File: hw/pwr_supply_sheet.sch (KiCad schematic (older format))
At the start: 15 parts

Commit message: PCB was too big for itead, reduced size and ordered one
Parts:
- C10, C12: footprint usevolt:usevolt-CAP_EEE-FK1H470P -> usevolt:CAP_EEE-FK1H470P
- D1: footprint usevolt:usevolt-DO-214AA -> usevolt:DO-214AA
- D2: footprint usevolt:usevolt-DO219AB -> usevolt:DO219AB
- F1: footprint usevolt:usevolt-FUSE_MC36211 -> usevolt:FUSE_MC36211
- L1: footprint usevolt:usevolt-INDUCTOR_BOURNS_10X13X5MM -> usevolt:INDUCTOR_BOURNS_10X13X5MM
- VR1: footprint usevolt:usevolt-SOIC8 -> usevolt:SOIC8
- VR2: footprint usevolt:usevolt-SOT-23_3-PIN -> usevolt:SOT-23_3-PIN
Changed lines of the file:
@@
 F 0 "F1" H 2600 4054 45  0000 C CNN
 F 1 "FUSE_MC36211_350MA" H 2600 3970 45  0000 C CNN
-F 2 "usevolt:usevolt-FUSE_MC36211" H 2630 4000 20  0001 C CNN
+F 2 "usevolt:FUSE_MC36211" H 2630 4000 20  0001 C CNN
 F 3 "http://www.farnell.com/datasheets/1678471.pdf?_ga=1.218604761.1948984246.1460023966" H 2720 3870 60  0001 C CNN
 F 4 "Farnell" H 3020 4170 60  0001 C CNN "1st Source"
@@
 F 0 "D1" V 3092 3982 45  0000 R CNN
 F 1 "DIODE_TVS_SMBJ33A-TRDO-214AA" V 3008 3982 45  0000 R CNN
-F 2 "usevolt:usevolt-DO-214AA" H 3030 4200 20  0001 C CNN
+F 2 "usevolt:DO-214AA" H 3030 4200 20  0001 C CNN
 F 3 "http://www.littelfuse.com/~/media/electronics/datasheets/tvs_diodes/littelfuse_tvs_diode_smbj_datasheet.pdf.pdf" H 3110 4060 60  0001 C CNN
 F 4 "Digi-Key" H 3410 4360 60  0001 C CNN "1st Source"
@@
 F 0 "C10" V 3308 4153 45  0000 L CNN
 F 1 "CAP_EEE-FK1H470P" V 3392 4153 45  0000 L CNN
-F 2 "usevolt:usevolt-CAP_EEE-FK1H470P" H 3430 4200 20  0001 C CNN
+F 2 "usevolt:CAP_EEE-FK1H470P" H 3430 4200 20  0001 C CNN
 F 3 "http://industrial.panasonic.com/www-cgi/jvcr13pz.cgi?E+PZ+3+ABA0120+EEEFK1H470P+7+WW" H 3400 3990 60  0001 C CNN
 F 4 "667-EEE-FK1H470P" H 4000 4590 60  0001 C CNN "2nd Source Part Number"
@@
 F 0 "VR1" H 5050 4804 45  0000 C CNN
 F 1 "LM2671SOIC8" H 5050 4720 45  0000 C CNN
-F 2 "usevolt:usevolt-SOIC8" H 4880 4300 20  0001 C CNN
+F 2 "usevolt:SOIC8" H 4880 4300 20  0001 C CNN
 F 3 "http://www.farnell.com/datasheets/1902681.pdf?_ga=1.246738500.1948984246.1460023966" H 4650 4670 60  0001 C CNN
 F 4 "1469200" H 5050 5070 60  0001 C CNN "1st Source Part Number"
@@
 F 0 "D2" V 6150 3852 45  0000 R CNN
 F 1 "DIODE_RS07J-GS18" H 6220 3890 45  0001 L BNN
-F 2 "usevolt:usevolt-DO219AB" H 6230 4100 20  0001 C CNN
+F 2 "usevolt:DO219AB" H 6230 4100 20  0001 C CNN
 F 3 "http://www.vishay.com/docs/85742/rs07b.pdf" H 6220 3970 60  0001 C CNN
 F 4 "1864882" H 6820 4570 60  0001 C CNN "2nd Source Part Number"
@@
 F 0 "L1" H 6500 4041 45  0000 C CNN
 F 1 "INDUCTOR_SDR1005-101KL" H 6500 3957 45  0000 C CNN
-F 2 "usevolt:usevolt-INDUCTOR_BOURNS_10X13X5MM" H 6530 4000 20  0001 C CNN
+F 2 "usevolt:INDUCTOR_BOURNS_10X13X5MM" H 6530 4000 20  0001 C CNN
 F 3 "http://www.farnell.com/datasheets/1695384.pdf?_ga=1.223340891.1948984246.1460023966" H 6400 3790 60  0001 C CNN
 F 4 "1828057" H 6800 4190 60  0001 C CNN "1st Source Part Number"
@@
 F 0 "C12" V 6758 4153 45  0000 L CNN
 F 1 "CAP_EEE-FK1H470P" V 6842 4153 45  0000 L CNN
-F 2 "usevolt:usevolt-CAP_EEE-FK1H470P" H 6880 4200 20  0001 C CNN
+F 2 "usevolt:CAP_EEE-FK1H470P" H 6880 4200 20  0001 C CNN
 F 3 "http://industrial.panasonic.com/www-cgi/jvcr13pz.cgi?E+PZ+3+ABA0120+EEEFK1H470P+7+WW" H 6850 3990 60  0001 C CNN
 F 4 "667-EEE-FK1H470P" H 7450 4590 60  0001 C CNN "2nd Source Part Number"
@@
 F 0 "VR2" H 8000 4305 45  0000 C CNN
 F 1 "REG_MCP1700" H 8000 3950 45  0001 L BNN
-F 2 "usevolt:usevolt-SOT-23_3-PIN" H 8030 4100 20  0001 C CNN
+F 2 "usevolt:SOT-23_3-PIN" H 8030 4100 20  0001 C CNN
 F 3 "http://www.farnell.com/datasheets/1784514.pdf?_ga=1.221693144.1948984246.1460023966" H 7700 4270 60  0001 C CNN
 F 4 "1296592" H 8100 4670 60  0001 C CNN "1st Source Part Number"

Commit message: starting to design hw 5.0, with variable current source for LCD backlight
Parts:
- removed C10, C12: CAP_EEE-FK1H470P, usevolt:CAP_EEE-FK1H470P, symbol CAP_EEE-FK1H470P
- removed D3: WL-SMCW-150060BS75000-B, wurth_LEDS:Wuerth_Elektronik_LEDs_rev15b-0603, symbol WL-SMCW-150060BS75000-B
- removed L1: INDUCTOR_SDR1005-101KL, usevolt:INDUCTOR_BOURNS_10X13X5MM, symbol INDUCTOR_SDR1005-101KL
- removed R4: 470, multicomp:Multicomp-RESC1608X60N, symbol 470
- added C201, C202: T491D226K035AT, kemet:7343, symbol T491D226K035AT
- added L201: IND_744045210, usevolt:IND_744045210, symbol IND_744045210
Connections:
- wire segments 31 -> 29
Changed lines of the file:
@@
 P 3000 4050
 F 0 "D1" V 3092 3982 45  0000 R CNN
-F 1 "DIODE_TVS_SMBJ33A-TRDO-214AA" V 3008 3982 45  0000 R CNN
+F 1 "DIODE_TVS_SMBJ33A-TRDO-214AA" V 2950 5150 45  0000 R CNN
 F 2 "usevolt:DO-214AA" H 3030 4200 20  0001 C CNN
 F 3 "http://www.littelfuse.com/~/media/electronics/datasheets/tvs_diodes/littelfuse_tvs_diode_smbj_datasheet.pdf.pdf" H 3110 4060 60  0001 C CNN
@@
 F 7 "KEMET" H 3204 4059 60  0001 C CNN "Manufacturer"
 	1    3200 3950
-	0    1    1    0
-$EndComp
-$Comp
-L CAP_EEE-FK1H470P C10
-U 1 1 57B821E6
-P 3400 4050
-F 0 "C10" V 3308 4153 45  0000 L CNN
-F 1 "CAP_EEE-FK1H470P" V 3392 4153 45  0000 L CNN
-F 2 "usevolt:CAP_EEE-FK1H470P" H 3430 4200 20  0001 C CNN
-F 3 "http://industrial.panasonic.com/www-cgi/jvcr13pz.cgi?E+PZ+3+ABA0120+EEEFK1H470P+7+WW" H 3400 3990 60  0001 C CNN
-F 4 "667-EEE-FK1H470P" H 4000 4590 60  0001 C CNN "2nd Source Part Number"
-F 5 "Digi-Key" H 3700 4290 60  0001 C CNN "1st Source"
-F 6 "EEE-FK1H470P" H 3600 4190 60  0001 C CNN "Manufacturer Part Number"
-F 7 "Mouser" H 3900 4490 60  0001 C CNN "2nd Source"
-F 8 "Panasonic Electronic Components" H 3500 4090 60  0001 C CNN "Manufacturer"
-F 9 "PCE3815CT-ND" H 3800 4390 60  0001 C CNN "1st Source Part Number"
-	1    3400 4050
 	0    1    1    0
 $EndComp
@@
 $EndComp
 $Comp
-L INDUCTOR_SDR1005-101KL L1
-U 1 1 57B82455
-P 6500 3850
-F 0 "L1" H 6500 4041 45  0000 C CNN
-F 1 "INDUCTOR_SDR1005-101KL" H 6500 3957 45  0000 C CNN
-F 2 "usevolt:INDUCTOR_BOURNS_10X13X5MM" H 6530 4000 20  0001 C CNN
-F 3 "http://www.farnell.com/datasheets/1695384.pdf?_ga=1.223340891.1948984246.1460023966" H 6400 3790 60  0001 C CNN
-F 4 "1828057" H 6800 4190 60  0001 C CNN "1st Source Part Number"
-F 5 "BOURNS" H 6500 3890 60  0001 C CNN "Manufacturer"
-F 6 "Digi-Key" H 6900 4290 60  0001 C CNN "2nd Source"
-F 7 "Farnell" H 6700 4090 60  0001 C CNN "1st Source"
-F 8 "SDR1005-101KL" H 6600 3990 60  0001 C CNN "Manufacturer Part Number"
-F 9 "SDR1005-101KLCT-ND" H 7000 4390 60  0001 C CNN "2nd Source Part Number"
-	1    6500 3850
-	1    0    0    -1
-$EndComp
-$Comp
-L CAP_EEE-FK1H470P C12
-U 1 1 57B827AB
-P 6850 4050
-F 0 "C12" V 6758 4153 45  0000 L CNN
-F 1 "CAP_EEE-FK1H470P" V 6842 4153 45  0000 L CNN
-F 2 "usevolt:CAP_EEE-FK1H470P" H 6880 4200 20  0001 C CNN
-F 3 "http://industrial.panasonic.com/www-cgi/jvcr13pz.cgi?E+PZ+3+ABA0120+EEEFK1H470P+7+WW" H 6850 3990 60  0001 C CNN
-F 4 "667-EEE-FK1H470P" H 7450 4590 60  0001 C CNN "2nd Source Part Number"
-F 5 "Digi-Key" H 7150 4290 60  0001 C CNN "1st Source"
-F 6 "EEE-FK1H470P" H 7050 4190 60  0001 C CNN "Manufacturer Part Number"
-F 7 "Mouser" H 7350 4490 60  0001 C CNN "2nd Source"
-F 8 "Panasonic Electronic Components" H 6950 4090 60  0001 C CNN "Manufacturer"
-F 9 "PCE3815CT-ND" H 7250 4390 60  0001 C CNN "1st Source Part Number"
-	1    6850 4050
-	0    1    1    0
-$EndComp
-$Comp
 L REG_MCP1700 VR2
 U 1 1 57B82857
@@
 	0    1    1    0
 $EndComp
-$Comp
-L 470 R4
-U 1 1 57B82ADF
-P 8850 3850
-F 0 "R4" V 8858 3908 45  0000 L CNN
-F 1 "470" V 8942 3908 45  0000 L CNN
-F 2 "multicomp:Multicomp-RESC1608X60N" H 8880 4000 20  0001 C CNN
-F 3 "" H 8819 3889 60  0001 C CNN
-F 4 "9331239" H 9219 4289 60  0001 C CNN "1st Source Part Number"
-F 5 "Farnell" H 9119 4189 60  0001 C CNN "1st Source"
-F 6 "MC0063W06031470R" H 9019 4089 60  0001 C CNN "Manufacturer Part Number"
-F 7 "MULTICOMP" H 8919 3989 60  0001 C CNN "Manufacturer"
-	1    8850 3850
-	0    1    1    0
-$EndComp
-$Comp
-L WL-SMCW-150060BS75000-B D3
-U 1 1 57B82B6E
-P 8850 4200
-F 0 "D3" V 8850 4132 45  0000 R CNN
-F 1 "WL-SMCW-150060BS75000-B" H 9050 4300 45  0001 L BNN
-F 2 "wurth_LEDS:Wuerth_Elektronik_LEDs_rev15b-0603" H 8880 4350 20  0001 C CNN
-F 3 "http://www.farnell.com/datasheets/1911343.pdf?_ga=1.259491274.1948984246.1460023966" H 8650 4400 60  0001 C CNN
-F 4 "150060BS75000" H 9059 4403 60  0001 C CNN "Manufacturer Part Number"
-F 5 "2322069" H 9259 4603 60  0001 C CNN "1st Source Part Number"
-F 6 "Farnell" H 9159 4503 60  0001 C CNN "1st Source"
-F 7 "WURTH ELEKTRONIK" H 8959 4303 60  0001 C CNN "Manufacturer"
-	1    8850 4200
-	0    -1   -1   0
-$EndComp
-Wire Wire Line
-	8850 4100 8850 4050
-Wire Wire Line
-	2900 4300 8850 4300
 Wire Wire Line
 	8000 4300 8000 4250
@@
 Connection ~ 3200 3850
 Wire Wire Line
-	8600 4150 8600 4300
-Connection ~ 8600 4300
-Wire Wire Line
-	8850 3750 8600 3750
-Wire Wire Line
 	8600 3600 8600 3850
 Wire Wire Line
@@
 	3400 3550 3400 3850
 $Comp
-L VDD #PWR020
+L VDD #PWR201
 U 1 1 57B83157
 P 3400 3550
-F 0 "#PWR020" H 3400 3400 50  0001 C CNN
+F 0 "#PWR201" H 3400 3400 50  0001 C CNN
 F 1 "VDD" H 3417 3723 50  0000 C CNN
 F 2 "" H 3400 3550 50  0000 C CNN
@@
 Connection ~ 3400 3750
 $Comp
-L +5V #PWR021
+L +5V #PWR204
 U 1 1 57B831F8
 P 6850 3600
-F 0 "#PWR021" H 6850 3450 50  0001 C CNN
+F 0 "#PWR204" H 6850 3450 50  0001 C CNN
 F 1 "+5V" H 6865 3773 50  0000 C CNN
 F 2 "" H 6850 3600 50  0000 C CNN
@@
 Connection ~ 6850 3750
 $Comp
-L +3V3 #PWR022
+L +3V3 #PWR205
 U 1 1 57B83259
 P 8600 3600
-F 0 "#PWR022" H 8600 3450 50  0001 C CNN
+F 0 "#PWR205" H 8600 3450 50  0001 C CNN
 F 1 "+3V3" H 8615 3773 50  0000 C CNN
 F 2 "" H 8600 3600 50  0000 C CNN
@@
 	1    0    0    -1
 $EndComp
-Connection ~ 8600 3750
 Wire Wire Line
 	2400 3850 2150 3850
@@
 NoConn ~ 4550 4050
 $Comp
-L VDD #PWR023
+L VDD #PWR202
 U 1 1 57B9C56A
 P 3800 2100
-F 0 "#PWR023" H 3800 1950 50  0001 C CNN
+F 0 "#PWR202" H 3800 1950 50  0001 C CNN
 F 1 "VDD" H 3817 2273 50  0000 C CNN
 F 2 "" H 3800 2100 50  0000 C CNN
@@
 $EndComp
 $Comp
-L PWR_FLAG #FLG024
+L PWR_FLAG #FLG201
 U 1 1 57B9C59C
 P 3800 2300
-F 0 "#FLG024" H 3800 2395 50  0001 C CNN
+F 0 "#FLG201" H 3800 2395 50  0001 C CNN
 F 1 "PWR_FLAG" H 3800 2523 50  0000 C CNN
 F 2 "" H 3800 2300 50  0000 C CNN
@@
 	3800 2300 3800 2100
 $Comp
-L GND #PWR025
+L GND #PWR203
 U 1 1 57B9D351
 P 4300 2350
-F 0 "#PWR025" H 4300 2100 50  0001 C CNN
+F 0 "#PWR203" H 4300 2100 50  0001 C CNN
 F 1 "GND" H 4305 2177 50  0000 C CNN
 F 2 "" H 4300 2350 50  0000 C CNN
@@
 $EndComp
 $Comp
-L PWR_FLAG #FLG026
+L PWR_FLAG #FLG202
 U 1 1 57B9D3A1
 P 4300 2150
-F 0 "#FLG026" H 4300 2245 50  0001 C CNN
+F 0 "#FLG202" H 4300 2245 50  0001 C CNN
 F 1 "PWR_FLAG" H 4300 2374 50  0000 C CNN
 F 2 "" H 4300 2150 50  0000 C CNN
@@
 Wire Wire Line
 	4300 2150 4300 2350
+Wire Wire Line
+	8600 4150 8600 4300
+Wire Wire Line
+	8600 4300 2900 4300
+$Comp
+L IND_744045210 L201
+U 1 1 58F3C600
+P 6500 3850
+F 0 "L201" H 6650 3900 45  0000 C CNN
+F 1 "IND_744045210" H 6500 3800 45  0000 C CNN
+F 2 "usevolt:IND_744045210" H 6530 4000 20  0001 C CNN
+F 3 "http://www.farnell.com/datasheets/1735442.pdf?_ga=1.223184091.1948984246.1460023966" H 6400 3790 60  0001 C CNN
+F 4 "1800416" H 6800 4190 60  0001 C CNN "1st Source Part Number"
+F 5 "WURTH ELEKTRONIK" H 6500 3890 60  0001 C CNN "Manufacturer"
+F 6 "Digi-Key" H 6900 4290 60  0001 C CNN "2nd Source"
+F 7 "Farnell" H 6700 4090 60  0001 C CNN "1st Source"
+F 8 "744045210" H 6600 3990 60  0001 C CNN "Manufacturer Part Number"
+F 9 "732-3072-1-ND" H 7000 4390 60  0001 C CNN "2nd Source Part Number"
+	1    6500 3850
+	1    0    0    -1
+$EndComp
+$Comp
+L T491D226K035AT C202
+U 1 1 58F3D3AB
+P 6850 4050
+F 0 "C202" V 6758 4153 45  0000 L CNN
+F 1 "T491D226K035AT" V 6842 4153 45  0000 L CNN
+F 2 "kemet:7343" H 6880 4200 20  0001 C CNN
+F 3 "http://www.farnell.com/datasheets/2121523.pdf?_ga=1.259966538.1948984246.1460023966" H 6850 3990 60  0001 C CNN
+F 4 "399-8375-1-ND" H 7450 4590 60  0001 C CNN "2nd Source Part Number"
+F 5 "Farnell" H 7150 4290 60  0001 C CNN "1st Source"
+F 6 "T491D226K035AT" H 7050 4190 60  0001 C CNN "Manufacturer Part Number"
+F 7 "Digikey" H 7350 4490 60  0001 C CNN "2nd Source"
+F 8 "Kemet" H 6950 4090 60  0001 C CNN "Manufacturer"
+F 9 "1457504" H 7250 4390 60  0001 C CNN "1st Source Part Number"
+	1    6850 4050
+	0    1    1    0
+$EndComp
+$Comp
+L T491D226K035AT C201
+U 1 1 58F3D42E
+P 3400 4050
+F 0 "C201" V 3308 4153 45  0000 L CNN
+F 1 "T491D226K035AT" V 3392 4153 45  0000 L CNN
+F 2 "kemet:7343" H 3430 4200 20  0001 C CNN
+F 3 "http://www.farnell.com/datasheets/2121523.pdf?_ga=1.259966538.1948984246.1460023966" H 3400 3990 60  0001 C CNN
+F 4 "399-8375-1-ND" H 4000 4590 60  0001 C CNN "2nd Source Part Number"
+F 5 "Farnell" H 3700 4290 60  0001 C CNN "1st Source"
+F 6 "T491D226K035AT" H 3600 4190 60  0001 C CNN "Manufacturer Part Number"
+F 7 "Digikey" H 3900 4490 60  0001 C CNN "2nd Source"
+F 8 "Kemet" H 3500 4090 60  0001 C CNN "Manufacturer"
+F 9 "1457504" H 3800 4390 60  0001 C CNN "1st Source Part Number"
+	1    3400 4050
+	0    1    1    0
+$EndComp
 $EndSCHEMATC

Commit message: still implementing treeview, not ready
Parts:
- removed R2: 10K, multicomp:Multicomp-RESC1608X60N, symbol 10K
- removed R3: 1K, multicomp:Multicomp-RESC1608X60N, symbol 1K
- added F201: FUSE_MC36211_350MA, usevolt:FUSE_MC36211, symbol FUSE_MC36211_350MA
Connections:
- net VIN: now also F201.P$1
- new net VLCD: F201.P$2
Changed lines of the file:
@@
 Wire Wire Line
 	2400 3850 2150 3850
-$Comp
-L 10K R2
-U 1 1 57B83930
-P 4100 3800
-F 0 "R2" V 4108 3858 45  0000 L CNN
-F 1 "10K" V 4192 3858 45  0000 L CNN
-F 2 "multicomp:Multicomp-RESC1608X60N" H 4130 3950 20  0001 C CNN
-F 3 "http://www.farnell.com/datasheets/1788326.pdf?_ga=1.214208087.1948984246.1460023966" H 4069 3839 60  0001 C CNN
-F 4 "9330399" H 4469 4239 60  0001 C CNN "1st Source Part Number"
-F 5 "Farnell" H 4369 4139 60  0001 C CNN "1st Source"
-F 6 "MC0063W0603110K" H 4269 4039 60  0001 C CNN "Manufacturer Part Number"
-F 7 "MULTICOMP" H 4169 3939 60  0001 C CNN "Manufacturer"
-	1    4100 3800
-	0    1    1    0
-$EndComp
-$Comp
-L 1K R3
-U 1 1 57B83997
-P 4100 4100
-F 0 "R3" V 4108 4158 45  0000 L CNN
-F 1 "1K" V 4192 4158 45  0000 L CNN
-F 2 "multicomp:Multicomp-RESC1608X60N" H 4130 4250 20  0001 C CNN
-F 3 "" H 4069 4139 60  0001 C CNN
-F 4 "9330380" H 4469 4539 60  0001 C CNN "1st Source Part Number"
-F 5 "Farnell" H 4369 4439 60  0001 C CNN "1st Source"
-F 6 "MC0063W060311K" H 4269 4339 60  0001 C CNN "Manufacturer Part Number"
-F 7 "MULTICOMP" H 4169 4239 60  0001 C CNN "Manufacturer"
-	1    4100 4100
-	0    1    1    0
-$EndComp
-Connection ~ 4100 4300
 Wire Wire Line
 	3400 3700 4550 3700
@@
 	4550 3700 4550 3750
 Connection ~ 3400 3700
-Connection ~ 4100 3700
-Text HLabel 4300 3400 2    60   Input ~ 0
-VDD_SENSE
-Wire Wire Line
-	4300 3400 4300 4000
-Wire Wire Line
-	4300 4000 4100 4000
 Text HLabel 7050 3600 2    60   Input ~ 0
 +5V
@@
 	0    1    1    0
 $EndComp
+$Comp
+L FUSE_MC36211_350MA F201
+U 1 1 58F5D8A5
+P 2600 3550
+F 0 "F201" H 2600 3754 45  0000 C CNN
+F 1 "FUSE_MC36211_350MA" H 2600 3670 45  0000 C CNN
+F 2 "usevolt:FUSE_MC36211" H 2630 3700 20  0001 C CNN
+F 3 "http://www.farnell.com/datasheets/1678471.pdf?_ga=1.218604761.1948984246.1460023966" H 2720 3570 60  0001 C CNN
+F 4 "Farnell" H 3020 3870 60  0001 C CNN "1st Source"
+F 5 "MC36211" H 2920 3770 60  0001 C CNN "Manufacturer Part Number"
+F 6 "MC36211" H 3120 3970 60  0001 C CNN "1st Source Part Number"
+F 7 "Multicomp" H 2820 3670 60  0001 C CNN "Manufacturer"
+	1    2600 3550
+	1    0    0    -1
+$EndComp
+Wire Wire Line
+	2400 3550 2200 3550
+Wire Wire Line
+	2200 3550 2200 3850
+Connection ~ 2200 3850
+Text HLabel 2950 3550 2    60   Output ~ 0
+VLCD
+Wire Wire Line
+	2950 3550 2800 3550
 $EndSCHEMATC

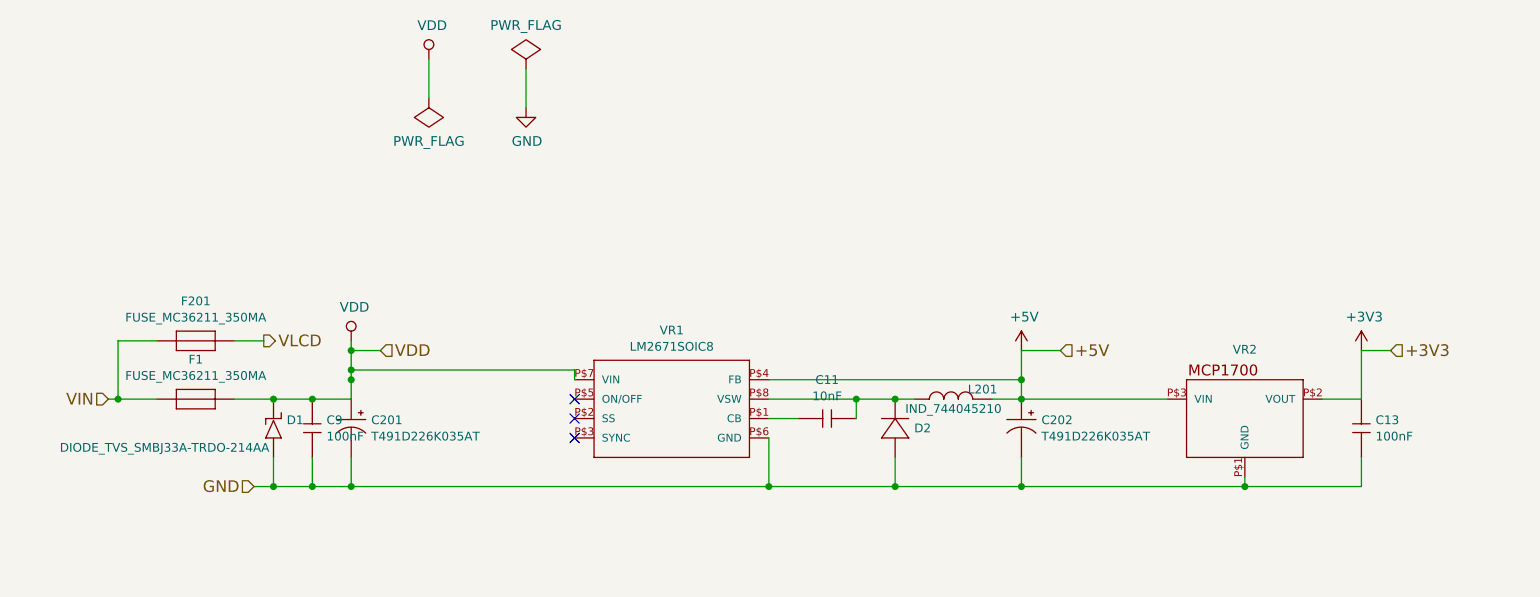
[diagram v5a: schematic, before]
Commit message: hw 1.5.0 ordered
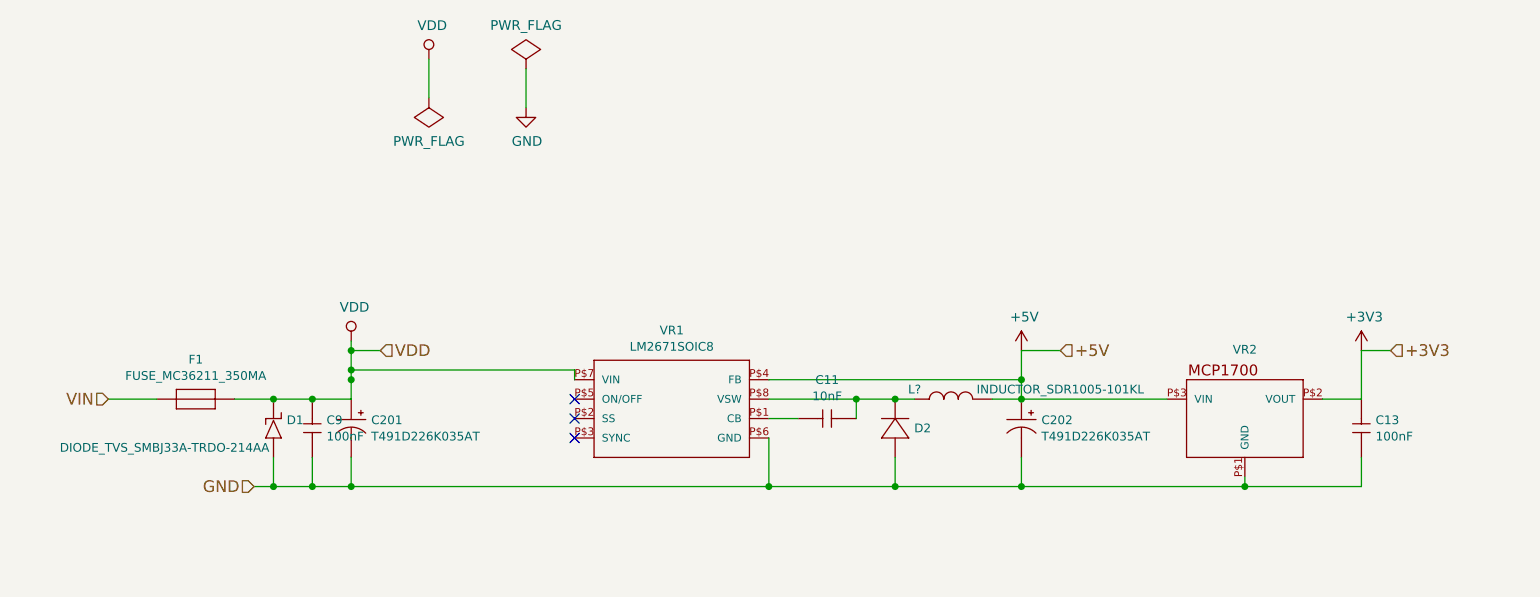
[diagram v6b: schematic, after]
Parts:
- removed F201: FUSE_MC36211_350MA, usevolt:FUSE_MC36211, symbol FUSE_MC36211_350MA
- removed L201: IND_744045210, usevolt:IND_744045210, symbol IND_744045210
- added L?: INDUCTOR_SDR1005-101KL, usevolt:INDUCTOR_BOURNS_10X13X5MM, symbol INDUCTOR_SDR1005-101KL
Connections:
- net +5V: now also L?.P$2
- net at C11.2 (C2), D2.P$2 (N), VR1.P$8 (VSW): now also L?.P$1
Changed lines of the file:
@@
 	8600 4300 2900 4300
-$Comp
-L IND_744045210 L201
-U 1 1 58F3C600
-P 6500 3850
-F 0 "L201" H 6650 3900 45  0000 C CNN
-F 1 "IND_744045210" H 6500 3800 45  0000 C CNN
-F 2 "usevolt:IND_744045210" H 6530 4000 20  0001 C CNN
-F 3 "http://www.farnell.com/datasheets/1735442.pdf?_ga=1.223184091.1948984246.1460023966" H 6400 3790 60  0001 C CNN
-F 4 "1800416" H 6800 4190 60  0001 C CNN "1st Source Part Number"
-F 5 "WURTH ELEKTRONIK" H 6500 3890 60  0001 C CNN "Manufacturer"
-F 6 "Digi-Key" H 6900 4290 60  0001 C CNN "2nd Source"
-F 7 "Farnell" H 6700 4090 60  0001 C CNN "1st Source"
-F 8 "744045210" H 6600 3990 60  0001 C CNN "Manufacturer Part Number"
-F 9 "732-3072-1-ND" H 7000 4390 60  0001 C CNN "2nd Source Part Number"
-	1    6500 3850
-	1    0    0    -1
-$EndComp
 $Comp
 L T491D226K035AT C202
@@
 $EndComp
 $Comp
-L FUSE_MC36211_350MA F201
-U 1 1 58F5D8A5
-P 2600 3550
-F 0 "F201" H 2600 3754 45  0000 C CNN
-F 1 "FUSE_MC36211_350MA" H 2600 3670 45  0000 C CNN
-F 2 "usevolt:FUSE_MC36211" H 2630 3700 20  0001 C CNN
-F 3 "http://www.farnell.com/datasheets/1678471.pdf?_ga=1.218604761.1948984246.1460023966" H 2720 3570 60  0001 C CNN
-F 4 "Farnell" H 3020 3870 60  0001 C CNN "1st Source"
-F 5 "MC36211" H 2920 3770 60  0001 C CNN "Manufacturer Part Number"
-F 6 "MC36211" H 3120 3970 60  0001 C CNN "1st Source Part Number"
-F 7 "Multicomp" H 2820 3670 60  0001 C CNN "Manufacturer"
-	1    2600 3550
+L INDUCTOR_SDR1005-101KL L?
+U 1 1 58FFA1B5
+P 6500 3850
+F 0 "L?" H 6300 3900 45  0000 C CNN
+F 1 "INDUCTOR_SDR1005-101KL" H 7050 3900 45  0000 C CNN
+F 2 "usevolt:INDUCTOR_BOURNS_10X13X5MM" H 6530 4000 20  0001 C CNN
+F 3 "http://www.farnell.com/datasheets/1695384.pdf?_ga=1.223340891.1948984246.1460023966" H 6400 3790 60  0001 C CNN
+F 4 "1828057" H 6800 4190 60  0001 C CNN "1st Source Part Number"
+F 5 "BOURNS" H 6500 3890 60  0001 C CNN "Manufacturer"
+F 6 "Digi-Key" H 6900 4290 60  0001 C CNN "2nd Source"
+F 7 "Farnell" H 6700 4090 60  0001 C CNN "1st Source"
+F 8 "SDR1005-101KL" H 6600 3990 60  0001 C CNN "Manufacturer Part Number"
+F 9 "SDR1005-101KLCT-ND" H 7000 4390 60  0001 C CNN "2nd Source Part Number"
+	1    6500 3850
 	1    0    0    -1
 $EndComp
-Wire Wire Line
-	2400 3550 2200 3550
-Wire Wire Line
-	2200 3550 2200 3850
-Connection ~ 2200 3850
-Text HLabel 2950 3550 2    60   Output ~ 0
-VLCD
-Wire Wire Line
-	2950 3550 2800 3550
 $EndSCHEMATC
